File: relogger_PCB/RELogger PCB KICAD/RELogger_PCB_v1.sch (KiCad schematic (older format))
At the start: 51 parts, among them P1 EXTERNAL PSU, P10 VANE, P11 SERIAL, P12 SOFT_SERIAL, P13 D6_D7, P14 AC_IN, P15 ANEMOM2, P16 ANEMOM1, P17 HC12, P2 BATTERY, P22 A_IN_45, P23 AGND_GND, P3 SOLAR, P4 A_IN_01, P5 A_IN_23, P6 I2C_1, P7 AN_JMP, P8 V_EXT, P9 3V3_VREF, Q1 Q_PMOS_DGS, Q3 Q_NPN_CBE, SW1 CALIBRATE, U1 MCP3208

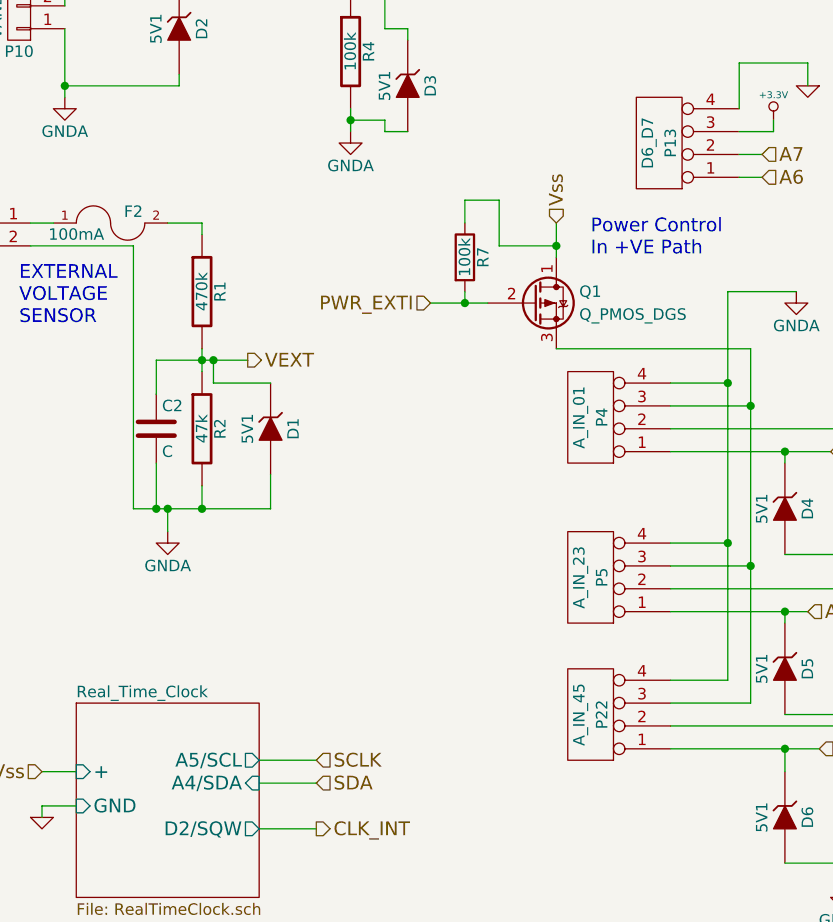
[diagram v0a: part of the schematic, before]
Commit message: Small updates
Battery voltage measurement
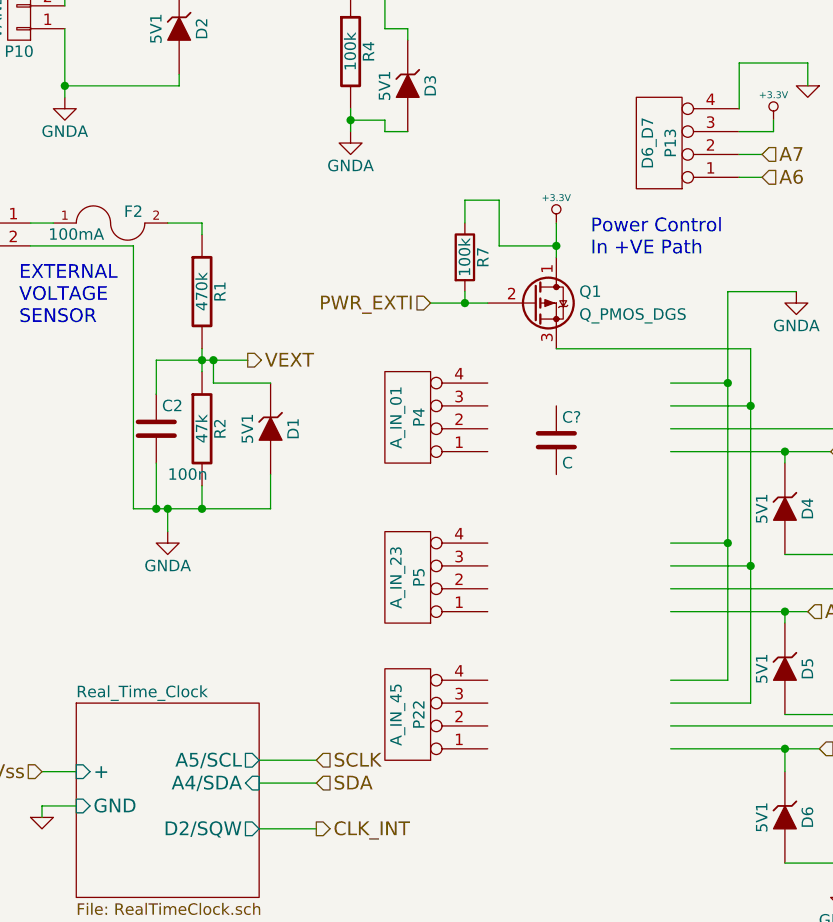
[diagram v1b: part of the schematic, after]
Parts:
- added C?: C, symbol C
- C2: value C -> 100n
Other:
- moved on the sheet: P22, P4, P5
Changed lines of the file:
@@
 L CONN_4 P4
 U 1 1 5464B8C5
-P 3500 5250
-F 0 "P4" V 3450 5250 50  0000 C CNN
-F 1 "A_IN_01" V 3550 5250 50  0000 C CNN
-F 2 "matts_components:SIL-4_Grove_SIL" H 3500 5250 60  0001 C CNN
-F 3 "" H 3500 5250 60  0000 C CNN
-F 4 "~" H 3500 5250 60  0001 C CNN "Description"
-F 5 "~" H 3500 5250 60  0001 C CNN "Notes"
-F 6 "~" H 3500 5250 60  0001 C CNN "Manufacturer"
-F 7 "~" H 3500 5250 60  0001 C CNN "Manufacturer Part No"
-F 8 "~" H 3500 5250 60  0001 C CNN "Supplier 1"
-F 9 "~" H 3500 5250 60  0001 C CNN "Supplier 1 Part No"
-F 10 "~" H 3500 5250 60  0001 C CNN "Supplier 2"
-F 11 "~" H 3500 5250 60  0001 C CNN "Supplier 2 Part No"
-F 12 "~" H 3500 5250 60  0001 C CNN "Cost"
-	1    3500 5250
+P 2700 5250
+F 0 "P4" V 2650 5250 50  0000 C CNN
+F 1 "A_IN_01" V 2750 5250 50  0000 C CNN
+F 2 "matts_components:SIL-4_Grove_SIL" H 2700 5250 60  0001 C CNN
+F 3 "" H 2700 5250 60  0000 C CNN
+F 4 "~" H 2700 5250 60  0001 C CNN "Description"
+F 5 "~" H 2700 5250 60  0001 C CNN "Notes"
+F 6 "~" H 2700 5250 60  0001 C CNN "Manufacturer"
+F 7 "~" H 2700 5250 60  0001 C CNN "Manufacturer Part No"
+F 8 "~" H 2700 5250 60  0001 C CNN "Supplier 1"
+F 9 "~" H 2700 5250 60  0001 C CNN "Supplier 1 Part No"
+F 10 "~" H 2700 5250 60  0001 C CNN "Supplier 2"
+F 11 "~" H 2700 5250 60  0001 C CNN "Supplier 2 Part No"
+F 12 "~" H 2700 5250 60  0001 C CNN "Cost"
+	1    2700 5250
 	-1   0    0    1
 $EndComp
@@
 L CONN_4 P5
 U 1 1 5464B8E3
-P 3500 5950
-F 0 "P5" V 3450 5950 50  0000 C CNN
-F 1 "A_IN_23" V 3550 5950 50  0000 C CNN
-F 2 "matts_components:SIL-4_Grove_SIL" H 3500 5950 60  0001 C CNN
-F 3 "" H 3500 5950 60  0000 C CNN
-F 4 "~" H 3500 5950 60  0001 C CNN "Description"
-F 5 "~" H 3500 5950 60  0001 C CNN "Notes"
-F 6 "~" H 3500 5950 60  0001 C CNN "Manufacturer"
-F 7 "~" H 3500 5950 60  0001 C CNN "Manufacturer Part No"
-F 8 "~" H 3500 5950 60  0001 C CNN "Supplier 1"
-F 9 "~" H 3500 5950 60  0001 C CNN "Supplier 1 Part No"
-F 10 "~" H 3500 5950 60  0001 C CNN "Supplier 2"
-F 11 "~" H 3500 5950 60  0001 C CNN "Supplier 2 Part No"
-F 12 "~" H 3500 5950 60  0001 C CNN "Cost"
-	1    3500 5950
+P 2700 5950
+F 0 "P5" V 2650 5950 50  0000 C CNN
+F 1 "A_IN_23" V 2750 5950 50  0000 C CNN
+F 2 "matts_components:SIL-4_Grove_SIL" H 2700 5950 60  0001 C CNN
+F 3 "" H 2700 5950 60  0000 C CNN
+F 4 "~" H 2700 5950 60  0001 C CNN "Description"
+F 5 "~" H 2700 5950 60  0001 C CNN "Notes"
+F 6 "~" H 2700 5950 60  0001 C CNN "Manufacturer"
+F 7 "~" H 2700 5950 60  0001 C CNN "Manufacturer Part No"
+F 8 "~" H 2700 5950 60  0001 C CNN "Supplier 1"
+F 9 "~" H 2700 5950 60  0001 C CNN "Supplier 1 Part No"
+F 10 "~" H 2700 5950 60  0001 C CNN "Supplier 2"
+F 11 "~" H 2700 5950 60  0001 C CNN "Supplier 2 Part No"
+F 12 "~" H 2700 5950 60  0001 C CNN "Cost"
+	1    2700 5950
 	-1   0    0    1
 $EndComp
@@
 	1650 5750 1650 5650
 Connection ~ 1650 5650
-$Comp
-L ZENER-RESCUE-RELogger_PCB_v1 D1
-U 1 1 57A777BA
-P 2100 5300
-F 0 "D1" H 2100 5400 50  0000 C CNN
-F 1 "5V1" H 2100 5200 50  0000 C CNN
-F 2 "REInnovationFootprint:TH_Diode_1" H 2100 5300 50  0001 C CNN
-F 3 "" H 2100 5300 50  0000 C CNN
-	1    2100 5300
-	0    1    1    0
-$EndComp
 $Comp
 L ZENER-RESCUE-RELogger_PCB_v1 D2
@@
 L CONN_4 P22
 U 1 1 58F4DB06
-P 3500 6550
-F 0 "P22" V 3450 6550 50  0000 C CNN
-F 1 "A_IN_45" V 3550 6550 50  0000 C CNN
-F 2 "matts_components:SIL-4_Grove_SIL" H 3500 6550 60  0001 C CNN
-F 3 "" H 3500 6550 60  0000 C CNN
-F 4 "~" H 3500 6550 60  0001 C CNN "Notes"
-F 5 "~" H 3500 6550 60  0001 C CNN "Description"
-F 6 "~" H 3500 6550 60  0001 C CNN "Manufacturer"
-F 7 "~" H 3500 6550 60  0001 C CNN "Manufacturer Part No"
-F 8 "~" H 3500 6550 60  0001 C CNN "Supplier 1"
-F 9 "~" H 3500 6550 60  0001 C CNN "Supplier 1 Part No"
-F 10 "~" H 3500 6550 60  0001 C CNN "Supplier 1 Cost"
-F 11 "~" H 3500 6550 60  0001 C CNN "Supplier 2"
-F 12 "~" H 3500 6550 60  0001 C CNN "Supplier 2 Part No"
-F 13 "~" H 3500 6550 60  0001 C CNN "Supplier 2 Cost"
-F 14 "~" H 3500 6550 60  0001 C CNN "Cost"
-	1    3500 6550
+P 2700 6550
+F 0 "P22" V 2650 6550 50  0000 C CNN
+F 1 "A_IN_45" V 2750 6550 50  0000 C CNN
+F 2 "matts_components:SIL-4_Grove_SIL" H 2700 6550 60  0001 C CNN
+F 3 "" H 2700 6550 60  0000 C CNN
+F 4 "~" H 2700 6550 60  0001 C CNN "Notes"
+F 5 "~" H 2700 6550 60  0001 C CNN "Description"
+F 6 "~" H 2700 6550 60  0001 C CNN "Manufacturer"
+F 7 "~" H 2700 6550 60  0001 C CNN "Manufacturer Part No"
+F 8 "~" H 2700 6550 60  0001 C CNN "Supplier 1"
+F 9 "~" H 2700 6550 60  0001 C CNN "Supplier 1 Part No"
+F 10 "~" H 2700 6550 60  0001 C CNN "Supplier 1 Cost"
+F 11 "~" H 2700 6550 60  0001 C CNN "Supplier 2"
+F 12 "~" H 2700 6550 60  0001 C CNN "Supplier 2 Part No"
+F 13 "~" H 2700 6550 60  0001 C CNN "Supplier 2 Cost"
+F 14 "~" H 2700 6550 60  0001 C CNN "Cost"
+	1    2700 6550
 	-1   0    0    1
 $EndComp
@@
 	7150 5550 7150 5650
 Connection ~ 6650 5550
-Text HLabel 3350 4400 1    60   Input ~ 0
-Vss
 Connection ~ 4200 5200
 Text HLabel 5500 4750 0    60   Input ~ 0
@@
 P 1600 5300
 F 0 "C2" H 1625 5400 50  0000 L CNN
-F 1 "C" H 1625 5200 50  0000 L CNN
+F 1 "100n" H 1650 5100 50  0000 L CNN
 F 2 "" H 1638 5150 50  0000 C CNN
 F 3 "" H 1600 5300 50  0000 C CNN
@@
 Wire Wire Line
 	10100 3650 10450 3650
+$Comp
+L +3.3V-RESCUE-RELogger_PCB_v1 #PWR?
+U 1 1 595E1E54
+P 3350 4400
+F 0 "#PWR?" H 3350 4360 30  0001 C CNN
+F 1 "+3.3V" H 3350 4510 30  0000 C CNN
+F 2 "" H 3350 4400 60  0000 C CNN
+F 3 "" H 3350 4400 60  0000 C CNN
+	1    3350 4400
+	1    0    0    -1
+$EndComp
+$Comp
+L ZENER-RESCUE-RELogger_PCB_v1 D1
+U 1 1 57A777BA
+P 2100 5300
+F 0 "D1" H 2100 5400 50  0000 C CNN
+F 1 "5V1" H 2100 5200 50  0000 C CNN
+F 2 "REInnovationFootprint:TH_Diode_1" H 2100 5300 50  0001 C CNN
+F 3 "" H 2100 5300 50  0000 C CNN
+	1    2100 5300
+	0    1    1    0
+$EndComp
+$Comp
+L C C?
+U 1 1 595EF852
+P 3350 5350
+F 0 "C?" H 3375 5450 50  0000 L CNN
+F 1 "C" H 3375 5250 50  0000 L CNN
+F 2 "" H 3388 5200 50  0000 C CNN
+F 3 "" H 3350 5350 50  0000 C CNN
+	1    3350 5350
+	1    0    0    -1
+$EndComp
 $EndSCHEMATC

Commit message: update
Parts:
- added C? (x2): 100n, symbol C
- added R? (x3): 4.7k, symbol R
- C?: value C -> 100n
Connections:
- wire segments 237 -> 251
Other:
- moved on the sheet: C?
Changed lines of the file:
@@
 $EndSheet
 $Sheet
-S 1250 6500 800  850
+S 1000 6400 800  850
 U 546244C3
 F0 "Real_Time_Clock" 50
 F1 "RealTimeClock.sch" 50
-F2 "A5/SCL" O R 2050 6750 60
-F3 "A4/SDA" I R 2050 6850 60
-F4 "+" I L 1250 6800 60
-F5 "GND" I L 1250 6950 60
-F6 "D2/SQW" O R 2050 7050 60
+F2 "A5/SCL" O R 1800 6650 60
+F3 "A4/SDA" I R 1800 6750 60
+F4 "+" I L 1000 6700 60
+F5 "GND" I L 1000 6850 60
+F6 "D2/SQW" O R 1800 6950 60
 $EndSheet
 $Sheet
@@
 L GND-RESCUE-RELogger_PCB_v1 #PWR05
 U 1 1 54647DB0
-P 1100 7000
-F 0 "#PWR05" H 1100 7000 30  0001 C CNN
-F 1 "GND" H 1100 6930 30  0001 C CNN
-F 2 "" H 1100 7000 60  0000 C CNN
-F 3 "" H 1100 7000 60  0000 C CNN
-	1    1100 7000
+P 850 6900
+F 0 "#PWR05" H 850 6900 30  0001 C CNN
+F 1 "GND" H 850 6830 30  0001 C CNN
+F 2 "" H 850 6900 60  0000 C CNN
+F 3 "" H 850 6900 60  0000 C CNN
+	1    850  6900
 	1    0    0    -1
 $EndComp
@@
 Text HLabel 10000 1900 0    60   Input ~ 0
 Vss
-Text HLabel 1100 6800 0    60   Input ~ 0
+Text HLabel 850  6700 0    60   Input ~ 0
 Vss
-Text HLabel 2300 6850 2    60   Input ~ 0
+Text HLabel 2050 6750 2    60   Input ~ 0
 SDA
-Text HLabel 2300 6750 2    60   Input ~ 0
+Text HLabel 2050 6650 2    60   Input ~ 0
 SCLK
-Text HLabel 2300 7050 2    60   Output ~ 0
+Text HLabel 2050 6950 2    60   Output ~ 0
 CLK_INT
 Text HLabel 6300 2750 2    60   Input ~ 0
@@
 	2750 950  2750 900
 Wire Wire Line
-	1250 6950 1100 6950
-Wire Wire Line
-	1100 6950 1100 7000
-Wire Wire Line
-	1250 6800 1100 6800
+	1000 6850 850  6850
+Wire Wire Line
+	850  6850 850  6900
+Wire Wire Line
+	1000 6700 850  6700
 Wire Wire Line
 	1750 1950 1650 1950
@@
 	4450 2850 4600 2850
 Wire Wire Line
-	2300 6850 2050 6850
-Wire Wire Line
-	2050 7050 2300 7050
+	2050 6750 1800 6750
+Wire Wire Line
+	1800 6950 2050 6950
 Text Notes 9000 1350 0    60   ~ 0
 Grove Connectors:\n1 - D0 / Rx / SCLK \n2 - D1 / Tx / SDA \n3 - V+\n4 - GND
@@
 SCK
 Wire Wire Line
-	2050 6750 2300 6750
+	1800 6650 2050 6650
 Text HLabel 6300 2850 2    60   Input ~ 0
 Tx
@@
 	5500 4550 5850 4550
 Wire Wire Line
-	3850 5100 4100 5100
-Wire Wire Line
-	4100 6400 3850 6400
-Wire Wire Line
-	4100 5800 3850 5800
+	3050 5100 4100 5100
+Wire Wire Line
+	3050 6400 4100 6400
+Wire Wire Line
+	3050 5800 4100 5800
 Connection ~ 4100 5800
 Wire Wire Line
-	3850 5200 4200 5200
-Wire Wire Line
-	4200 4950 4200 6500
-Wire Wire Line
-	4200 6500 3850 6500
-Wire Wire Line
-	3850 5900 4200 5900
+	3050 5200 4200 5200
+Wire Wire Line
+	4200 6500 4200 4950
+Wire Wire Line
+	3050 6500 4200 6500
+Wire Wire Line
+	3050 5900 4200 5900
 Connection ~ 4200 5900
 $Comp
@@
 $EndComp
 Wire Wire Line
-	3850 6100 4450 6100
-Wire Wire Line
-	3850 6000 4900 6000
+	3050 6000 4900 6000
 Connection ~ 4800 6000
 Wire Wire Line
-	3850 5400 4550 5400
-Wire Wire Line
-	3850 5300 4900 5300
+	3050 5300 4900 5300
 Wire Wire Line
 	4800 5350 4800 5300
@@
 	4800 7200 4800 7100
 Wire Wire Line
-	3850 6700 4500 6700
-Wire Wire Line
-	3850 6600 4900 6600
+	3050 6600 4900 6600
 Wire Wire Line
 	4800 6700 4800 6600
@@
 	2700 3550 2700 3600
 Wire Wire Line
-	4100 4700 4100 6400
+	4100 6400 4100 4700
 Wire Wire Line
 	9000 5550 9300 5550
@@
 Connection ~ 8850 4200
 Wire Wire Line
-	4400 4700 4100 4700
+	4100 4700 4400 4700
 $Comp
 L Q_PMOS_DGS Q1
@@
 $EndComp
 Wire Wire Line
-	3350 4550 3350 4400
-Wire Wire Line
-	3350 4950 4200 4950
+	3350 4400 3350 4550
+Wire Wire Line
+	4200 4950 3350 4950
 Wire Wire Line
 	2800 4750 3050 4750
@@
 L C C?
 U 1 1 595EF852
-P 3350 5350
-F 0 "C?" H 3375 5450 50  0000 L CNN
-F 1 "C" H 3375 5250 50  0000 L CNN
-F 2 "" H 3388 5200 50  0000 C CNN
-F 3 "" H 3350 5350 50  0000 C CNN
-	1    3350 5350
-	1    0    0    -1
-$EndComp
+P 3800 5650
+F 0 "C?" H 3825 5750 50  0000 L CNN
+F 1 "100n" H 3825 5550 50  0000 L CNN
+F 2 "" H 3838 5500 50  0000 C CNN
+F 3 "" H 3800 5650 50  0000 C CNN
+	1    3800 5650
+	0    -1   -1   0
+$EndComp
+$Comp
+L R R?
+U 1 1 595FA426
+P 3300 5400
+F 0 "R?" V 3380 5400 50  0000 C CNN
+F 1 "4.7k" V 3300 5400 50  0000 C CNN
+F 2 "" V 3230 5400 50  0000 C CNN
+F 3 "" H 3300 5400 50  0000 C CNN
+	1    3300 5400
+	0    1    1    0
+$EndComp
+$Comp
+L C C?
+U 1 1 595FBB16
+P 3800 6300
+F 0 "C?" H 3825 6400 50  0000 L CNN
+F 1 "100n" H 3825 6200 50  0000 L CNN
+F 2 "" H 3838 6150 50  0000 C CNN
+F 3 "" H 3800 6300 50  0000 C CNN
+	1    3800 6300
+	0    -1   -1   0
+$EndComp
+$Comp
+L C C?
+U 1 1 595FBD4A
+P 3800 6900
+F 0 "C?" H 3825 7000 50  0000 L CNN
+F 1 "100n" H 3825 6800 50  0000 L CNN
+F 2 "" H 3838 6750 50  0000 C CNN
+F 3 "" H 3800 6900 50  0000 C CNN
+	1    3800 6900
+	0    -1   -1   0
+$EndComp
+$Comp
+L R R?
+U 1 1 595FFC91
+P 3300 6100
+F 0 "R?" V 3380 6100 50  0000 C CNN
+F 1 "4.7k" V 3300 6100 50  0000 C CNN
+F 2 "" V 3230 6100 50  0000 C CNN
+F 3 "" H 3300 6100 50  0000 C CNN
+	1    3300 6100
+	0    1    1    0
+$EndComp
+$Comp
+L R R?
+U 1 1 595FFECB
+P 3300 6700
+F 0 "R?" V 3380 6700 50  0000 C CNN
+F 1 "4.7k" V 3300 6700 50  0000 C CNN
+F 2 "" V 3230 6700 50  0000 C CNN
+F 3 "" H 3300 6700 50  0000 C CNN
+	1    3300 6700
+	0    1    1    0
+$EndComp
+Wire Wire Line
+	3050 5400 3150 5400
+Wire Wire Line
+	3450 5400 4550 5400
+Wire Wire Line
+	3650 5650 3650 5400
+Connection ~ 3650 5400
+Wire Wire Line
+	3050 6100 3150 6100
+Wire Wire Line
+	3450 6100 4450 6100
+Wire Wire Line
+	3450 6700 4500 6700
+Wire Wire Line
+	3050 6700 3150 6700
+Wire Wire Line
+	3950 6300 4000 6300
+Wire Wire Line
+	4000 6300 4000 5800
+Connection ~ 4000 5800
+Wire Wire Line
+	3950 5650 4000 5650
+Wire Wire Line
+	4000 5650 4000 5100
+Connection ~ 4000 5100
+Wire Wire Line
+	3650 6300 3600 6300
+Wire Wire Line
+	3600 6300 3600 6100
+Connection ~ 3600 6100
+Wire Wire Line
+	3950 6900 4050 6900
+Wire Wire Line
+	4050 6900 4050 6400
+Connection ~ 4050 6400
+Wire Wire Line
+	3650 6900 3600 6900
+Wire Wire Line
+	3600 6900 3600 6700
+Connection ~ 3600 6700
 $EndSCHEMATC

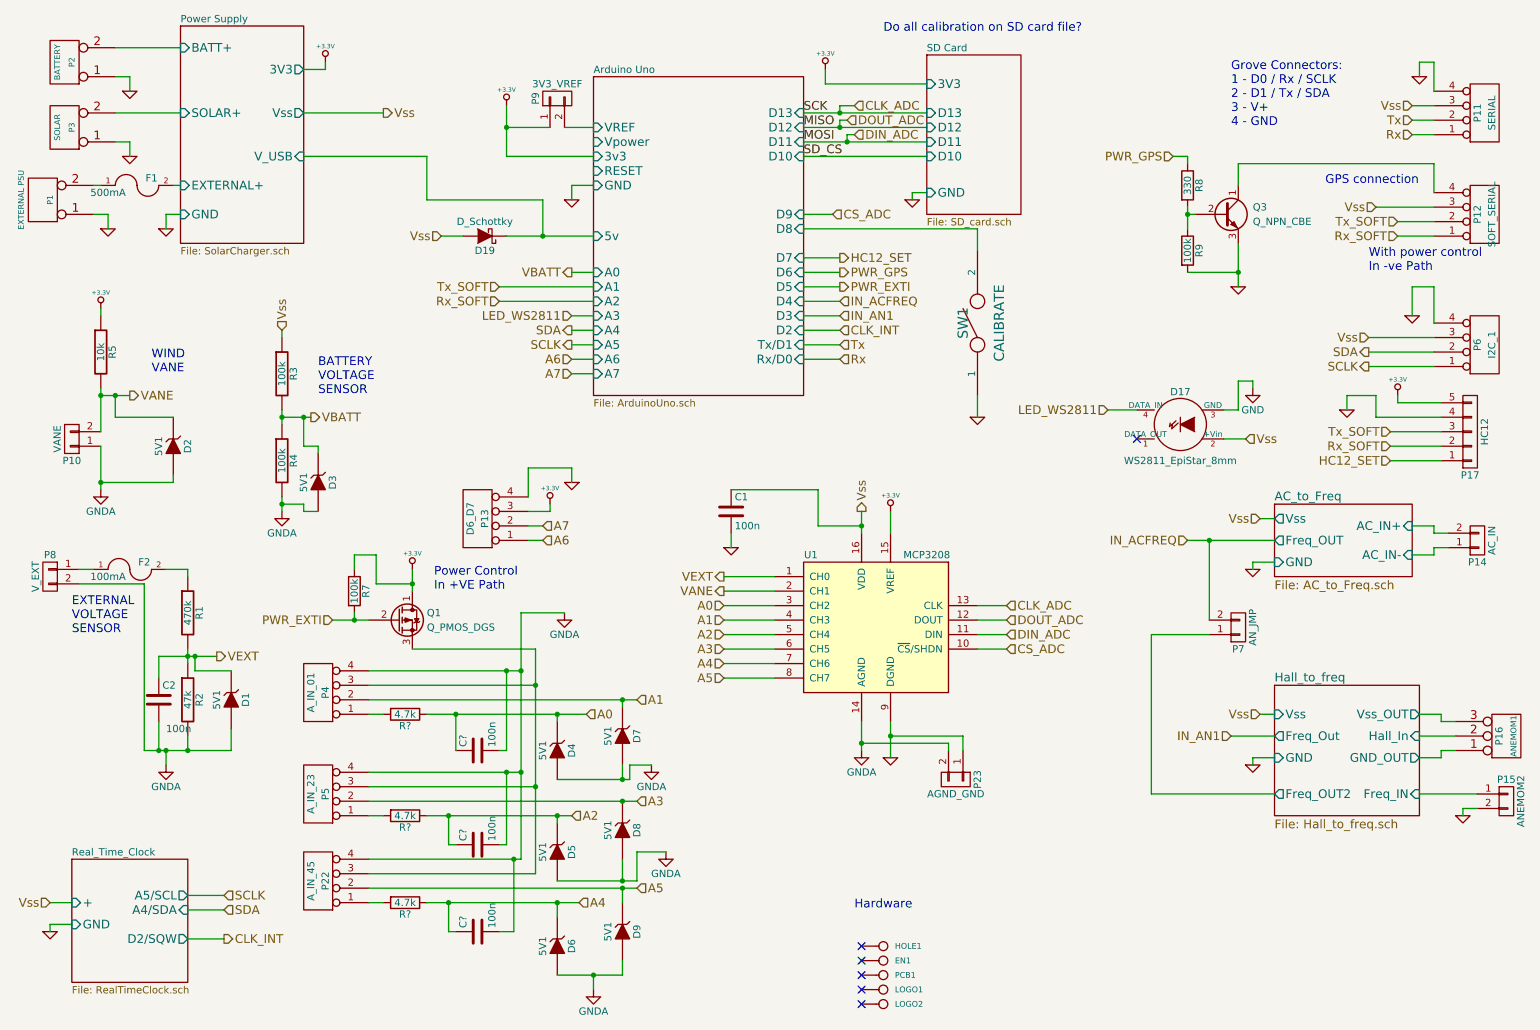
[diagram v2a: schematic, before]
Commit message: Updated new scehmatic.
Still needs Freq conversion circuit. And 3.3V regulator
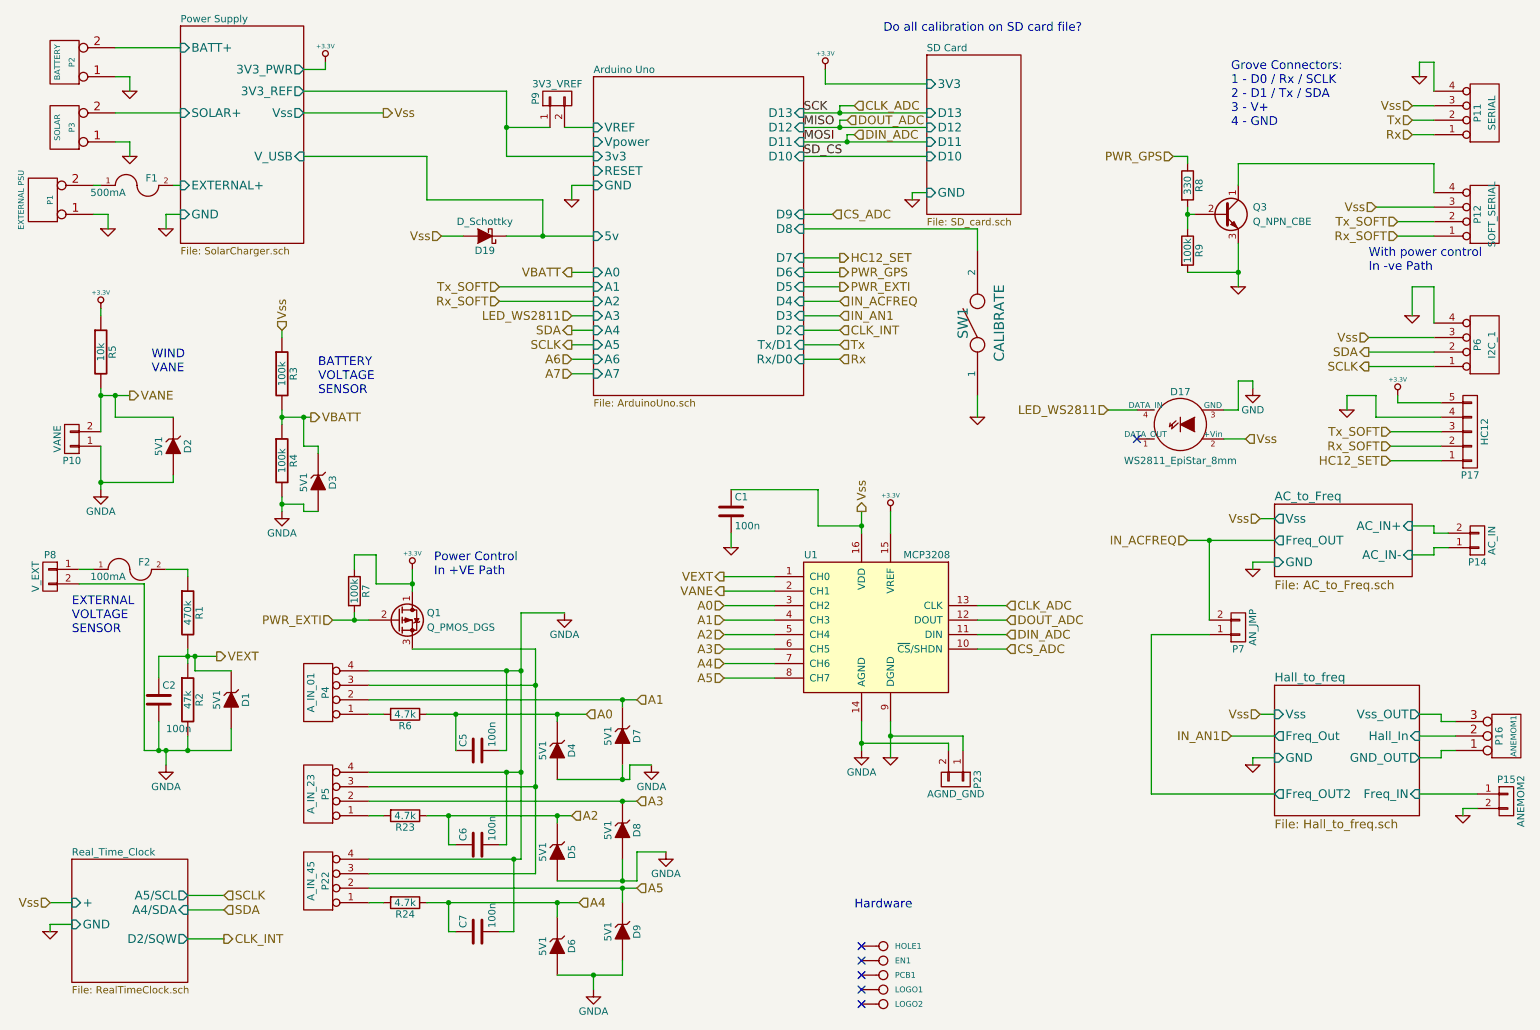
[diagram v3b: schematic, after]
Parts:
- removed P13: D6_D7, matts_components:SIL-4_Grove_SIL, symbol CONN_4
- gave numbers to parts that had none: 6
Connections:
- net +3.3V: no longer P9.1 (P1)
- new net Arduino Uno/3v3: P9.1 (P1)
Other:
- note removed: "GPS connection"
